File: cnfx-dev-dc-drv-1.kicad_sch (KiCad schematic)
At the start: 0 parts

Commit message: schem: import STM32F103 from mhadb-2208-bldc-drv
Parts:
- added C11, C12, C3, C6, C8: 0u1, Capacitor_SMD:C_0402_1005Metric, symbol Device:C
- added C13, C14: 1u, Capacitor_SMD:C_0402_1005Metric, symbol Device:C
- added C15: 10n, Capacitor_SMD:C_0402_1005Metric, symbol Device:C
- added C2: 10u, Capacitor_SMD:C_0805_2012Metric, symbol Device:C
- added C4, C5: 20p, Capacitor_SMD:C_0603_1608Metric, symbol Device:C
- added D11: YELLOW, LED_SMD:LED_0805_2012Metric, symbol Device:LED
- added FB1: 600Ω@100M, Inductor_SMD:L_0805_2012Metric, symbol Device:FerriteBead
- added R4, R5, R7: 10k, Resistor_SMD:R_0402_1005Metric, symbol Device:R
- added R6: 560, Resistor_SMD:R_0603_1608Metric, symbol Device:R_Small
- added R8: 5k1, Resistor_SMD:R_0402_1005Metric, symbol Device:R
- added TP1: TestPoint, TestPoint:TestPoint_Pad_D2.0mm, symbol Connector:TestPoint
- added U2: STM32F103C8Tx, Package_QFP:LQFP-48_7x7mm_P0.5mm, symbol MCU_ST_STM32F1:STM32F103C8Tx
- added Y1: 8M, Crystal:Crystal_SMD_5032-2Pin_5.0x3.2mm, symbol Device:Crystal
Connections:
- new net: R8.1, U2.38 (PA15)
- new net: D11.2 (A), R8.2
- new net: C14.1, C15.1, FB1.1, U2.9 (VDDA)
- new net +3V3: C11.1, C12.1, C13.1, C2.1, C6.1, C8.1, FB1.2, R5.2, R7.1, U2.1 (VBAT), U2.24 (VDD), U2.36 (VDD), U2.48 (VDD)
- new net BOOT: R4.2, U2.44 (BOOT0)
- new net BTN1: U2.41 (PB5)
- new net CAN_RX: U2.32 (PA11)
- new net CAN_TX: U2.33 (PA12)
- new net GND: C11.2, C12.2, C13.2, C14.2, C15.2, C2.2, C3.2, C4.2, C5.2, C6.2, C8.2, D11.1 (K), R4.1, U2.20 (PB2), U2.23 (VSS), U2.35 (VSS), U2.47 (VSS), U2.8 (VSSA)
- new net NRST: C3.1, TP1.1, U2.7 (NRST)
- new net SCL: R5.1, U2.42 (PB6)
- new net SDA: R7.2, U2.43 (PB7)
- new net SWCLK: U2.37 (PA14)
- new net SWDIO: U2.34 (PA13)
- new net SWO: U2.39 (PB3)
- new net XTAL_I: C4.1, U2.5 (PD0), Y1.2
- new net XTAL_O: R6.2, U2.6 (PD1)
- new net XTAL_RO: C5.1, R6.1, Y1.1
- no-connect marks 0 -> 11
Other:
- note added: "CAN Alive"
- note added: "HSE"

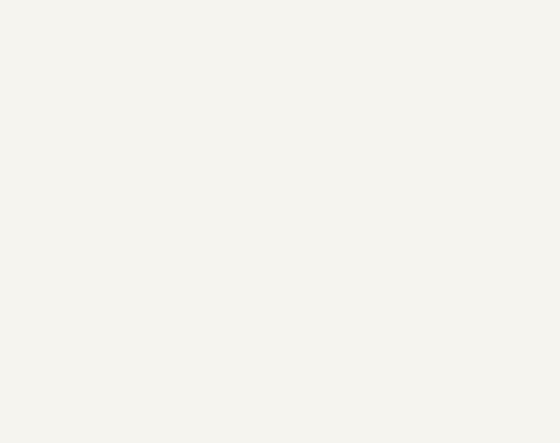
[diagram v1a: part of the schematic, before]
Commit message: schem: add BOOT/RST and misc btns
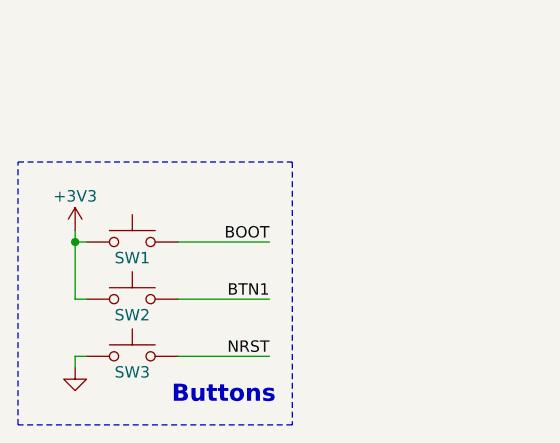
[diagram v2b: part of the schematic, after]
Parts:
- added SW1, SW2, SW3: SW_Push, Button_Switch_SMD:SW_SPST_TS-1088-xR020, symbol Switch:SW_Push
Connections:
- net +3V3: now also SW1.1, SW2.1
- net BOOT: now also SW1.2
- net BTN1: now also SW2.2
- net GND: now also SW3.1
- net NRST: now also SW3.2
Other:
- note added: "Buttons"

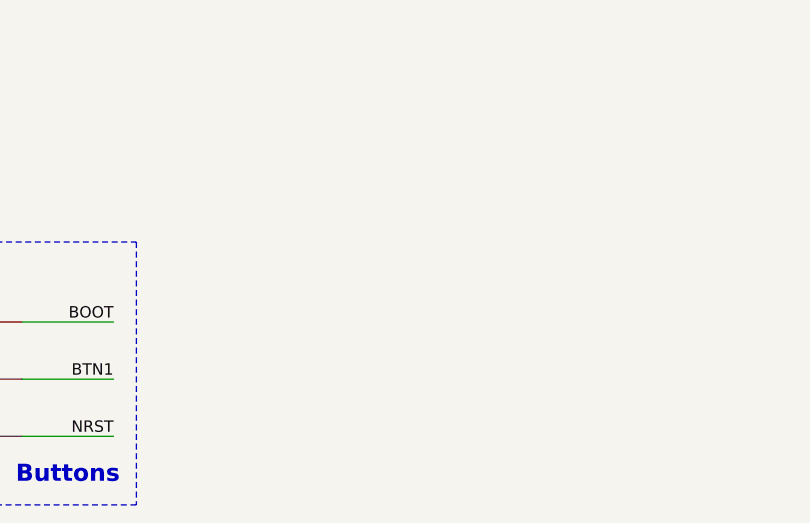
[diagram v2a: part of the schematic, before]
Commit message: schem: import TC2030 debug connector
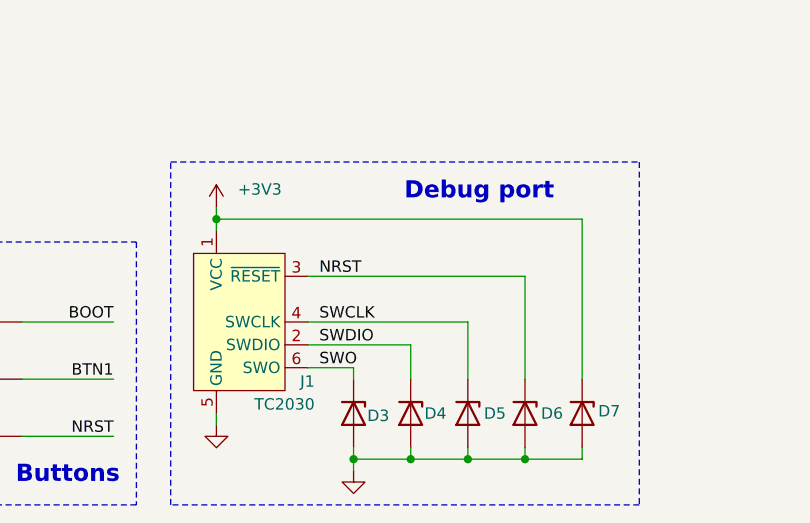
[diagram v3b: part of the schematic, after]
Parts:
- added D3, D4, D5, D6, D7: H5VU10U, GLCS:Diode_DFN1006, symbol GLCS:H5VU10U
- added J1: TC2030, Connector:Tag-Connect_TC2030-IDC-NL_2x03_P1.27mm_Vertical, symbol Connector:Conn_ARM_SWD_TagConnect_TC2030-NL
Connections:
- net +3V3: now also D7.1 (K), J1.1 (VCC)
- net GND: now also D3.2 (A), D4.2 (A), D5.2 (A), D6.2 (A), D7.2 (A), J1.5 (GND)
- net NRST: now also D6.1 (K), J1.3 (~{RESET})
- net SWCLK: now also D5.1 (K), J1.4 (SWCLK)
- net SWDIO: now also D4.1 (K), J1.2 (SWDIO)
- net SWO: now also D3.1 (K), J1.6 (SWO)
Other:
- note added: "Debug port"

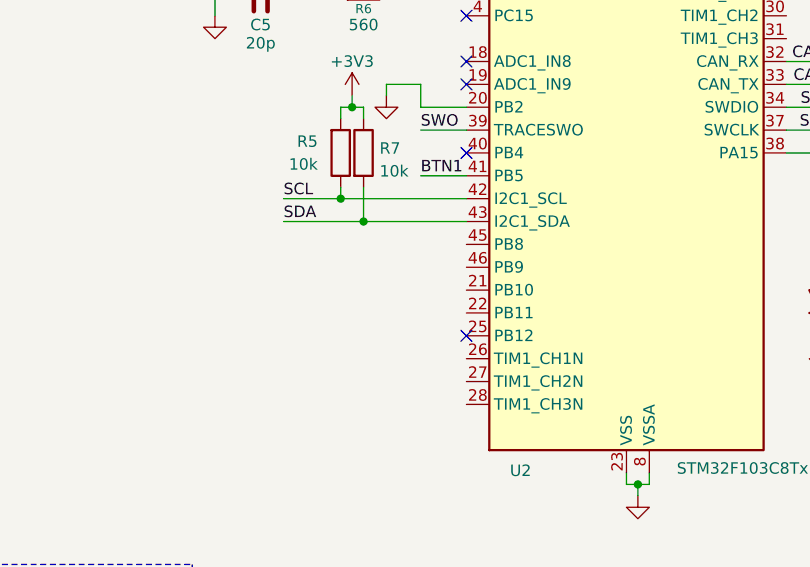
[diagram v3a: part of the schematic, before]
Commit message: schem: add spare gpios
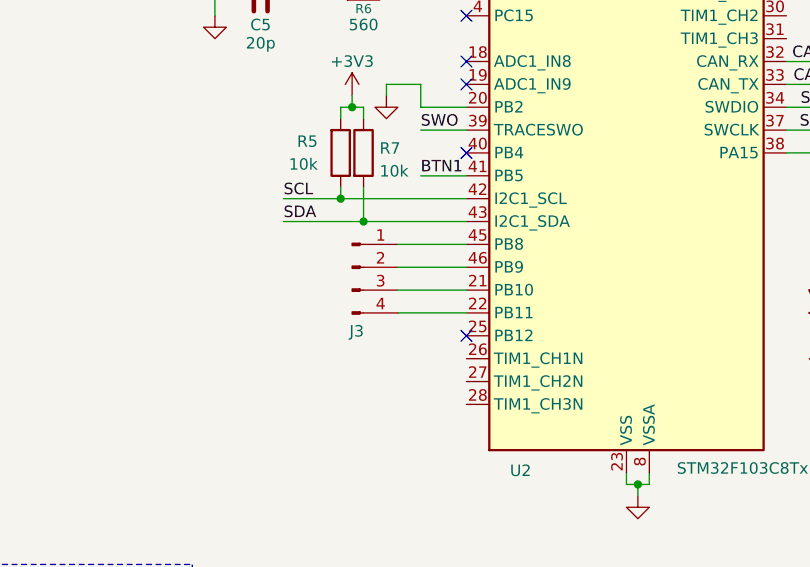
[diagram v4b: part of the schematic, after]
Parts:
- added J3: Conn_01x04_Pin, Connector_PinHeader_2.54mm:PinHeader_1x04_P2.54mm_Vertical, symbol Connector:Conn_01x04_Pin
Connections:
- net at U2.21 (PB10): now also J3.3 (Pin_3)
- net at U2.22 (PB11): now also J3.4 (Pin_4)
- net at U2.45 (PB8): now also J3.1 (Pin_1)
- net at U2.46 (PB9): now also J3.2 (Pin_2)
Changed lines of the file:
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@@
 	(wire
 		(pts
+			(xy 134.62 125.73) (xy 127 125.73)
+		)
+		(stroke
+			(width 0)
+			(type default)
+		)
+	)
+	(wire
+		(pts
 			(xy 91.44 189.23) (xy 91.44 187.96)
 		)
@@
 	(wire
 		(pts
+			(xy 134.62 128.27) (xy 127 128.27)
+		)
+		(stroke
+			(width 0)
+			(type default)
+		)
+	)
+	(wire
+		(pts
 			(xy 177.8 102.87) (xy 170.18 102.87)
 		)
@@
 	(wire
 		(pts
+			(xy 134.62 120.65) (xy 127 120.65)
+		)
+		(stroke
+			(width 0)
+			(type default)
+		)
+	)
+	(wire
+		(pts
 			(xy 25.4 173.99) (xy 24.13 173.99)
 		)
@@
 	(wire
 		(pts
+			(xy 134.62 123.19) (xy 127 123.19)
+		)
+		(stroke
+			(width 0)
+			(type default)
+		)
+	)
+	(wire
+		(pts
 			(xy 173.99 130.81) (xy 173.99 132.08)
 		)
@@
 					(unit 1)
 				)
+			)
+		)
+	)
+	(symbol
+		(lib_id "Connector:Conn_01x04_Pin")
+		(at 121.92 123.19 0)
+		(unit 1)
+		(body_style 1)
+		(exclude_from_sim no)
+		(in_bom no)
+		(on_board yes)
+		(in_pos_files yes)
+		(dnp no)
+		(property "Reference" "J3"
+			(at 122.428 130.302 0)
+			(show_name no)
+			(do_not_autoplace no)
+			(effects
+				(font
+					(size 1.27 1.27)
+				)
+			)
+		)
+		(property "Value" "Conn_01x04_Pin"
+			(at 119.38 124.46 90)
+			(hide yes)
+			(show_name no)
+			(do_not_autoplace no)
+			(effects
+				(font
+					(size 1.27 1.27)
+				)
+			)
+		)
+		(property "Footprint" "Connector_PinHeader_2.54mm:PinHeader_1x04_P2.54mm_Vertical"
+			(at 121.92 123.19 0)
+			(hide yes)
+			(show_name no)
+			(do_not_autoplace no)
+			(effects
+				(font
+					(size 1.27 1.27)
+				)
+			)
+		)
+		(property "Datasheet" ""
+			(at 121.92 123.19 0)
+			(hide yes)
+			(show_name no)
+			(do_not_autoplace no)
+			(effects
+				(font
+					(size 1.27 1.27)
+				)
+			)
+		)
+		(property "Description" "Generic connector, single row, 01x04, script generated"
+			(at 121.92 123.19 0)
+			(hide yes)
+			(show_name no)
+			(do_not_autoplace no)
+			(effects
+				(font
+					(size 1.27 1.27)
+				)
+			)
+		)
+		(pin "4"
+		)
+		(pin "3"
+		)
+		(pin "2"
+		)
+		(pin "1"
+		)
+		(instances
+			(project "cnfx-dev-dc-drv-1"
+				(path "/d7250a19-615d-468e-abbc-0dea4b78aeef"
+					(reference "J3")
+					(unit 1)
+				)

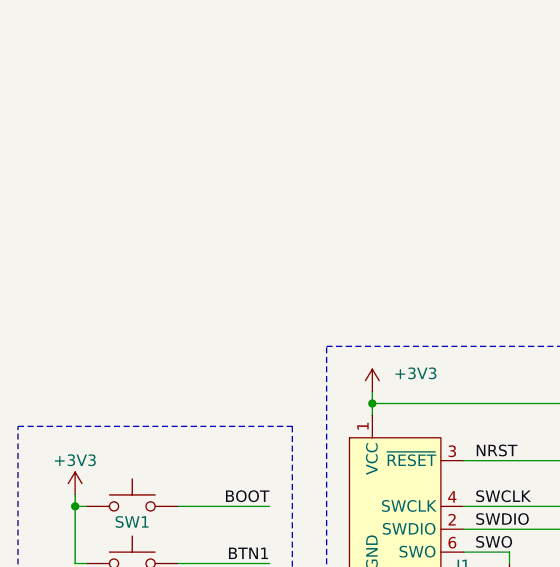
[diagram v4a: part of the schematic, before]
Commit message: schem: add RGB status led
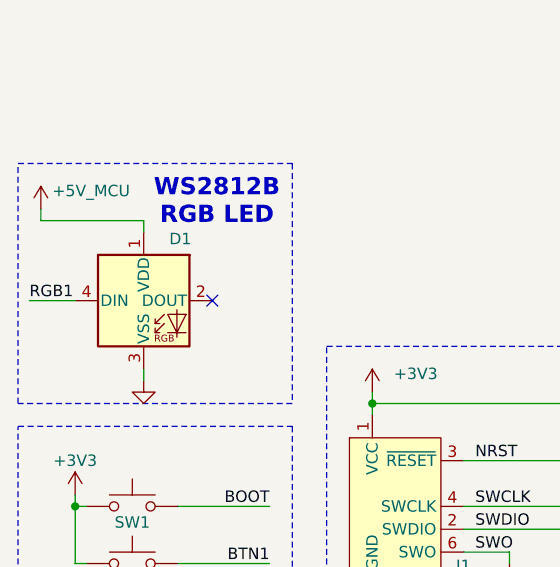
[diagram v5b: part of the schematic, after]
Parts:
- added D1: WS2812B, LED_SMD:LED_WS2812B_PLCC4_5.0x5.0mm_P3.2mm, symbol LED:WS2812B
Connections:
- net GND: now also D1.3 (VSS)
- new net +5V_MCU: D1.1 (VDD)
- new net RGB1: D1.4 (DIN)
- no-connect marks 11 -> 12
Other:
- note added: "WS2812B RGB LED"

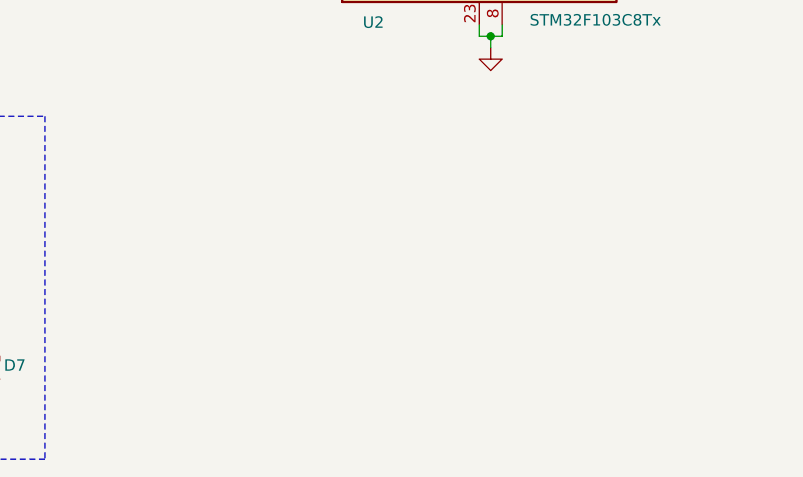
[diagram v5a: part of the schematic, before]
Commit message: schem: import CAN transceiver
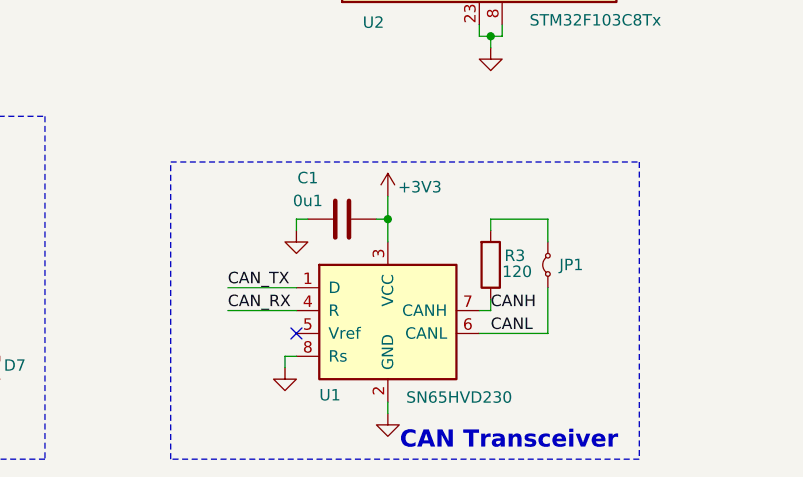
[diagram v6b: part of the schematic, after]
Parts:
- added C1: 0u1, Capacitor_SMD:C_0402_1005Metric, symbol Device:C
- added JP1: Jumper_2_Small_Bridged, Jumper:SolderJumper-2_P1.3mm_Open_RoundedPad1.0x1.5mm, symbol Jumper:Jumper_2_Small_Bridged
- added R3: 120, Resistor_SMD:R_1206_3216Metric, symbol Device:R
- added U1: SN65HVD230, Package_SO:SOIC-8_3.9x4.9mm_P1.27mm, symbol Interface_CAN_LIN:SN65HVD230
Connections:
- net +3V3: now also C1.1, U1.3 (VCC)
- net CAN_RX: now also U1.4 (R)
- net CAN_TX: now also U1.1 (D)
- net GND: now also C1.2, U1.2 (GND), U1.8 (Rs)
- new net: JP1.2 (B), R3.2
- new net CANH: R3.1, U1.7 (CANH)
- new net CANL: JP1.1 (A), U1.6 (CANL)
- no-connect marks 12 -> 13
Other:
- note added: "CAN Transceiver"

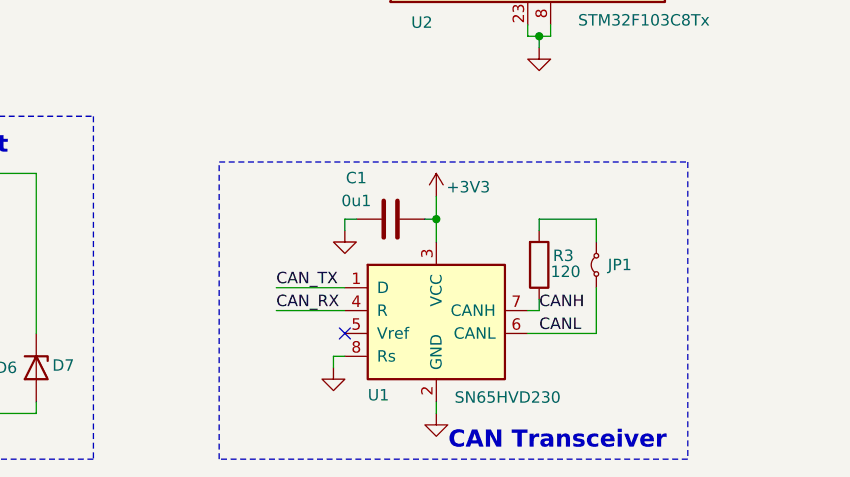
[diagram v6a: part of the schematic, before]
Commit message: schem: add CAN connectors
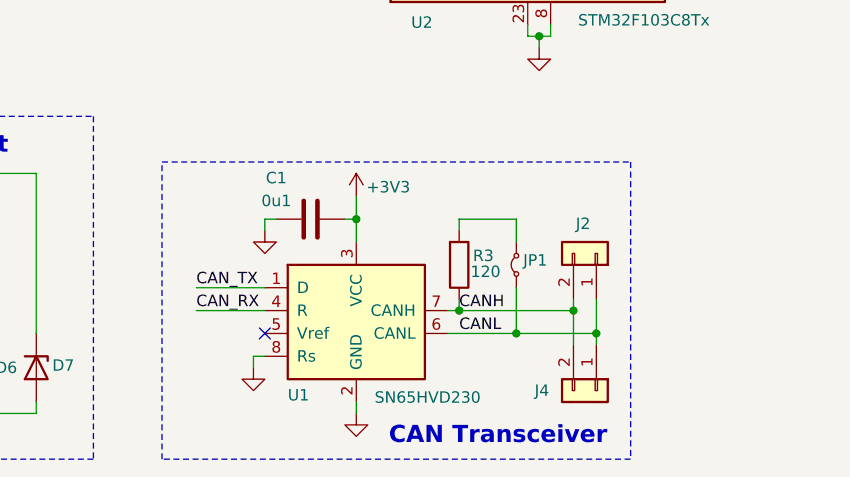
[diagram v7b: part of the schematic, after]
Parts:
- added J2, J4: Conn_01x02, Connector_JST:JST_XH_B2B-XH-A_1x02_P2.50mm_Vertical, symbol Connector_Generic:Conn_01x02
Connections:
- net CANH: now also J2.2 (Pin_2), J4.2 (Pin_2)
- net CANL: now also J2.1 (Pin_1), J4.1 (Pin_1)
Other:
- moved on the sheet: C1, JP1, R3, U1

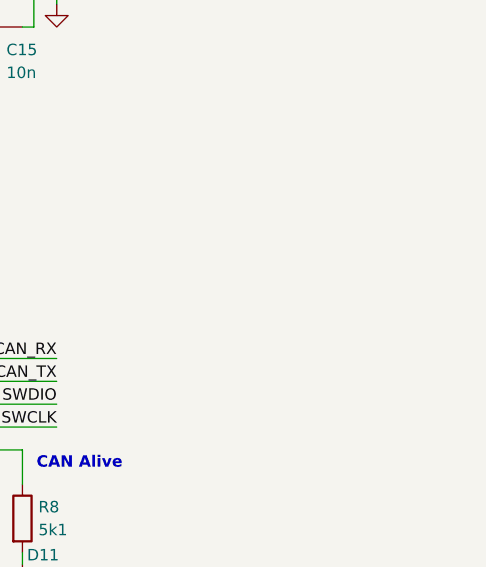
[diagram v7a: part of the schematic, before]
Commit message: schem: add DRV8837 dc motor drivers
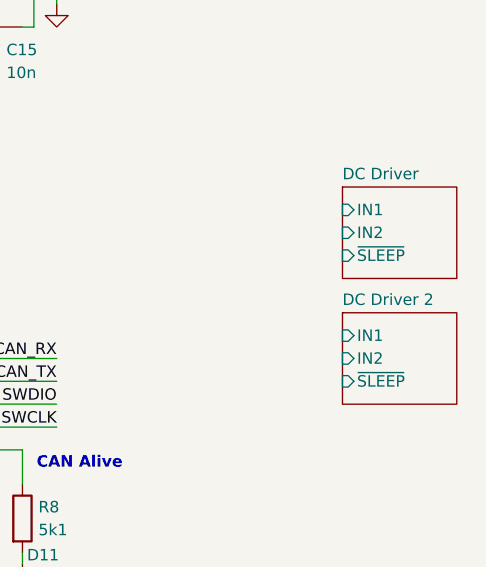
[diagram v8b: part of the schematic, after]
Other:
- added sheet DC Driver (dc-drv.kicad_sch)
- added sheet DC Driver 2 (dc-drv.kicad_sch)
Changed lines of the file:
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@@
+		)
+	)
+	(sheet
+		(at 209.55 95.25)
+		(size 12.7 10.16)
+		(exclude_from_sim no)
+		(in_bom yes)
+		(on_board yes)
+		(dnp no)
+		(fields_autoplaced yes)
+		(stroke
+			(width 0.1524)
+			(type solid)
+		)
+		(fill
+			(color 0 0 0 0)
+		)
+		(property "Sheetname" "DC Driver 2"
+			(at 209.55 94.5384 0)
+			(show_name no)
+			(do_not_autoplace no)
+			(effects
+				(font
+					(size 1.27 1.27)
+				)
+				(justify left bottom)
+			)
+		)
+		(property "Sheetfile" "dc-drv.kicad_sch"
+			(at 209.55 105.9946 0)
+			(hide yes)
+			(show_name no)
+			(do_not_autoplace no)
+			(effects
+				(font
+					(size 1.27 1.27)
+				)
+				(justify left top)
+			)
+		)
+		(pin "~{SLEEP}" input
+			(at 209.55 102.87 180)
+			(effects
+				(font
+					(size 1.27 1.27)
+				)
+				(justify left)
+			)
+		)
+		(pin "IN1" input
+			(at 209.55 97.79 180)
+			(effects
+				(font
+					(size 1.27 1.27)
+				)
+				(justify left)
+			)
+		)
+		(pin "IN2" input
+			(at 209.55 100.33 180)
+			(effects
+				(font
+					(size 1.27 1.27)
+				)
+				(justify left)
+			)
+		)
+		(instances
+			(project "cnfx-dev-dc-drv-1"
+				(path "/d7250a19-615d-468e-abbc-0dea4b78aeef"
+					(page "3")
+				)
+			)
+		)
+	)
+	(sheet
+		(at 209.55 81.28)
+		(size 12.7 10.16)
+		(exclude_from_sim no)
+		(in_bom yes)
+		(on_board yes)
+		(dnp no)
+		(fields_autoplaced yes)
+		(stroke
+			(width 0.1524)
+			(type solid)
+		)
+		(fill
+			(color 0 0 0 0)
+		)
+		(property "Sheetname" "DC Driver"
+			(at 209.55 80.5684 0)
+			(show_name no)
+			(do_not_autoplace no)
+			(effects
+				(font
+					(size 1.27 1.27)
+				)
+				(justify left bottom)
+			)
+		)
+		(property "Sheetfile" "dc-drv.kicad_sch"
+			(at 209.55 92.0246 0)
+			(hide yes)
+			(show_name no)
+			(do_not_autoplace no)
+			(effects
+				(font
+					(size 1.27 1.27)
+				)
+				(justify left top)
+			)
+		)
+		(pin "~{SLEEP}" input
+			(at 209.55 88.9 180)
+			(effects
+				(font
+					(size 1.27 1.27)
+				)
+				(justify left)
+			)
+		)
+		(pin "IN1" input
+			(at 209.55 83.82 180)
+			(effects
+				(font
+					(size 1.27 1.27)
+				)
+				(justify left)
+			)
+		)
+		(pin "IN2" input
+			(at 209.55 86.36 180)
+			(effects
+				(font
+					(size 1.27 1.27)
+				)
+				(justify left)
+			)
+		)
+		(instances
+			(project "cnfx-dev-dc-drv-1"
+				(path "/d7250a19-615d-468e-abbc-0dea4b78aeef"
+					(page "2")
+				)
+			)
 		)
 	)
